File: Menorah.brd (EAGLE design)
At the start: 100 x 80 mm, 0 parts

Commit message: design finished
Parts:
- added C1: 100uF, rcl:C1808
- added G1: CR2032V, battery:CR2032V
- added IC1: (no value), linear:SO08
- added LED1, LED2, LED3, LED4, LED5, LED6, LED7, LED8, LED9: (no value), led:P-LCC-4
- added R1, R2, R3, R4, R5, R6, R7, R8, R9: (no value), rcl:R0805
- added R10: 10M, rcl:R0805
- added R11: 50k, rcl:R0805
- added R12: 100k, rcl:R0805
- added S1, S2, S3, S4, S5, S6, S7, S8, S9: 2P2T, switch:2P2T
- added S10: RDT1034, switch:RDT1034
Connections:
- new net N$1: LED1.A, R1.2
- new net N$10: R1.1, S1.3.2
- new net N$11: R2.1, S2.3.2
- new net N$12: R3.1, S3.3.2
- new net N$13: R4.1, S4.3.2
- new net N$14: R5.1, S5.3.2
- new net N$15: R6.1, S6.3.2
- new net N$16: R7.1, S7.3.2
- new net N$17: R8.1, S8.3.2
- new net N$18: R9.1, S9.3.2
- new net N$19: IC1.2, R11.1, R12.2
- new net N$2: LED2.A, R2.2
- new net N$20: C1.1, IC1.3, R10.2, S10.B
- new net N$21: IC1.6, S1.2.1
- new net N$23: S1.2.2, S2.2.1
- new net N$24: S2.2.2, S3.2.1
- new net N$25: S3.2.2, S4.2.1
- new net N$26: S4.2.2, S5.2.1
- new net N$27: S5.2.2, S6.2.1
- new net N$28: S6.2.2, S7.2.1
- new net N$29: S7.2.2, S8.2.1
- new net N$3: LED3.A, R3.2
- new net N$30: S8.2.2, S9.2.1
- new net N$4: LED4.A, R4.2
- new net N$5: LED5.A, R5.2
- new net N$6: LED6.A, R6.2
- new net N$7: LED7.A, R7.2
- new net N$8: LED8.A, R8.2
- new net N$9: LED9.A, R9.2
- new net PE: C1.2, G1.-, IC1.4, LED1.C@4, LED2.C@4, LED3.C@4, LED4.C@4, LED5.C@4, LED6.C@4, LED7.C@4, LED8.C@4, LED9.C@4, R10.1, R11.2
- new net VCC: G1.+, IC1.7, R12.1, S10.A, S10.A1

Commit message: digikey part numbers added
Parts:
- C1: device rcl:C1808 -> rcl:C1206
- LED1, LED2, LED3, LED4, LED5, LED6, LED7, LED8: value (none) -> YELLOW; device led:P-LCC-4 -> led:CHIPLED_0805
- LED9: value (none) -> RED; device led:P-LCC-4 -> led:CHIPLED_0805
- R1, R2, R3, R4, R5, R6, R7, R8: value (none) -> 56
- R11: value 50k -> 51k
- R9: value (none) -> 68
- moved S3 275.9 mm to (-152.4, -255.3)
- moved S4 275.9 mm to (-152.4, -268.0)
- moved S5 275.9 mm to (-152.4, -280.7)
- moved S6 275.9 mm to (-152.4, -293.4)
- moved S9 275.9 mm to (-152.4, -331.5)
- moved S2 275.9 mm to (-152.4, -242.6)
- moved S7 275.9 mm to (-152.4, -306.1)
- moved S8 275.9 mm to (-152.4, -318.8)
- moved R8 179.5 mm to (-157.5, -233.7)
- moved R7 178.9 mm to (-157.5, -227.3)
- moved R6 178.3 mm to (-157.5, -221.0)
- moved R5 177.8 mm to (-157.5, -214.6)
- moved R4 177.2 mm to (-157.5, -208.3)
- moved R3 176.7 mm to (-157.5, -201.9)
- moved R2 176.2 mm to (-157.5, -195.6)
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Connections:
- net PE: now also LED1.C, LED2.C, LED3.C, LED4.C, LED5.C, LED6.C, LED7.C, LED8.C, LED9.C; no longer LED1.C@4, LED2.C@4, LED3.C@4, LED4.C@4, LED5.C@4, LED6.C@4, LED7.C@4, LED8.C@4, LED9.C@4

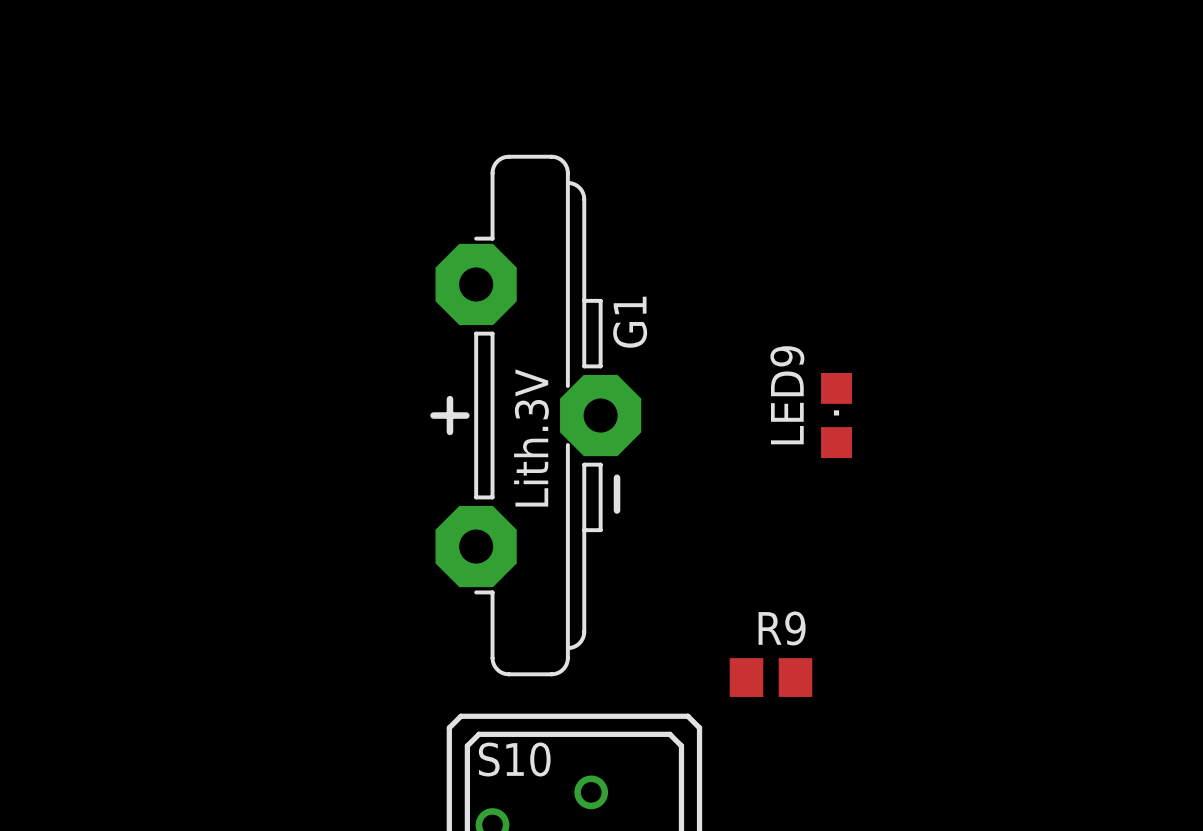
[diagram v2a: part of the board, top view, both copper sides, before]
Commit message: replaced cr2032
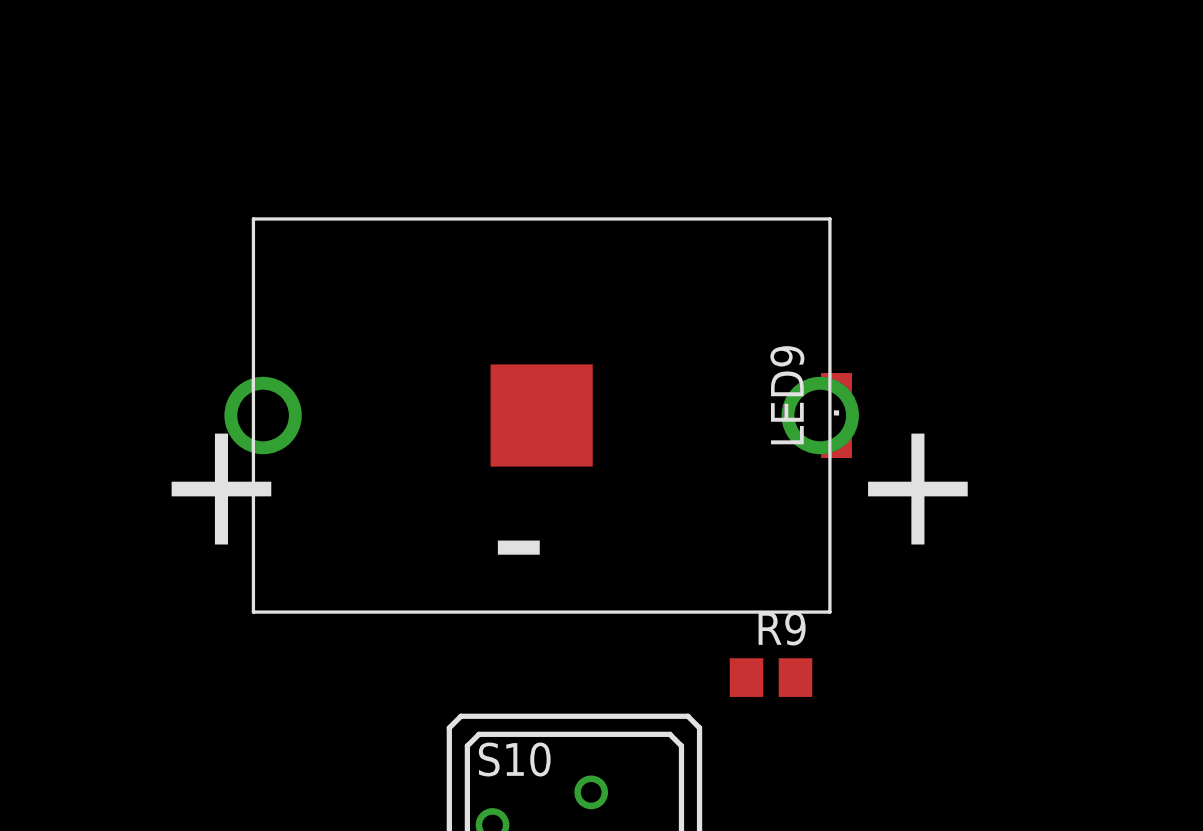
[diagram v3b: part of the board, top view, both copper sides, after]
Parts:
- G1: value CR2032V -> CR2032; device battery:CR2032V -> Menorah:BK-913
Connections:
- new net +: G1.+@1
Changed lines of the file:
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@@
 <attribute name="DIGIKEY" value="1276-5504-1-ND" x="-100.33" y="-157.48" size="1.778" layer="27" display="off"/>
 </element>
-<element name="G1" library="battery" package="CR2032V" value="CR2032V" x="-109.22" y="-147.32">
+<element name="G1" library="Menorah" package="BK-913" value="CR2032" x="-109.22" y="-147.32">
 <attribute name="DIGIKEY" value="BK-913-ND" x="-109.22" y="-147.32" size="1.778" layer="27" display="off"/>
+<attribute name="LAYOUT-VERIFIED" value="No" x="-109.22" y="-147.32" size="1.778" layer="27" display="off"/>
 </element>
 <element name="S10" library="switch" package="RDT1034" value="RDT1034" x="-107.95" y="-163.83">
 <attribute name="DIGIKEY" value="EG4791-ND" x="-107.95" y="-163.83" size="1.778" layer="27" display="off"/>
+<attribute name="LAYOUT-VERIFIED" value="No" x="-107.95" y="-163.83" size="1.778" layer="27" display="off"/>
 </element>
 <element name="C1" library="rcl" package="C1206" value="100uF" x="-110.49" y="-172.72">
@@
 <contactref element="LED7" pad="C"/>
 <contactref element="LED8" pad="C"/>
-<wire x1="-106.934" y1="-147.32" x2="-97.79" y2="-146.27" width="0" layer="19" extent="1-1"/>
-<wire x1="-109.09" y1="-172.72" x2="-106.934" y2="-147.32" width="0" layer="19" extent="1-1"/>
+<wire x1="-109.22" y1="-147.32" x2="-97.79" y2="-146.27" width="0" layer="19" extent="1-1"/>
+<wire x1="-109.09" y1="-172.72" x2="-109.22" y2="-147.32" width="0" layer="19" extent="1-1"/>
 <wire x1="-111.44" y1="-179.07" x2="-109.09" y2="-172.72" width="0" layer="19" extent="1-1"/>
 <wire x1="-109.54" y1="-184.15" x2="-111.44" y2="-179.07" width="0" layer="19" extent="1-1"/>
@@
 <wire x1="-111.125" y1="-163.195" x2="-118.745" y2="-177.74" width="0" layer="19" extent="1-1"/>
 <wire x1="-104.775" y1="-164.465" x2="-111.125" y2="-163.195" width="0" layer="19" extent="1-1"/>
-<wire x1="-111.76" y1="-152.4" x2="-111.125" y2="-163.195" width="0" layer="19" extent="1-1"/>
+<wire x1="-120.02" y1="-147.32" x2="-111.125" y2="-163.195" width="0" layer="19" extent="1-1"/>
 </signal>
 <signal name="N$19">
@@
 <wire x1="-152.4" y1="-321.42" x2="-152.4" y2="-328.82" width="0" layer="19" extent="1-1"/>
 </signal>
+<signal name="+">
+<contactref element="G1" pad="+@1"/>
+</signal>
 </signals>

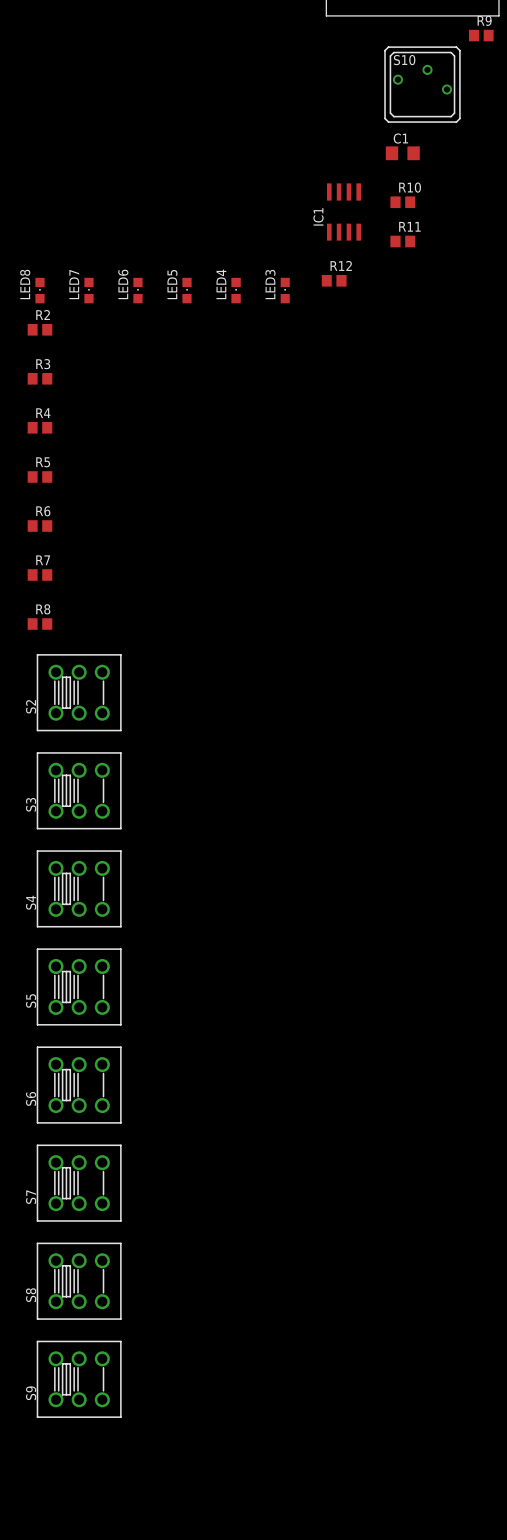
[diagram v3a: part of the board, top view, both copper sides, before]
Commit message: replaced spst switch
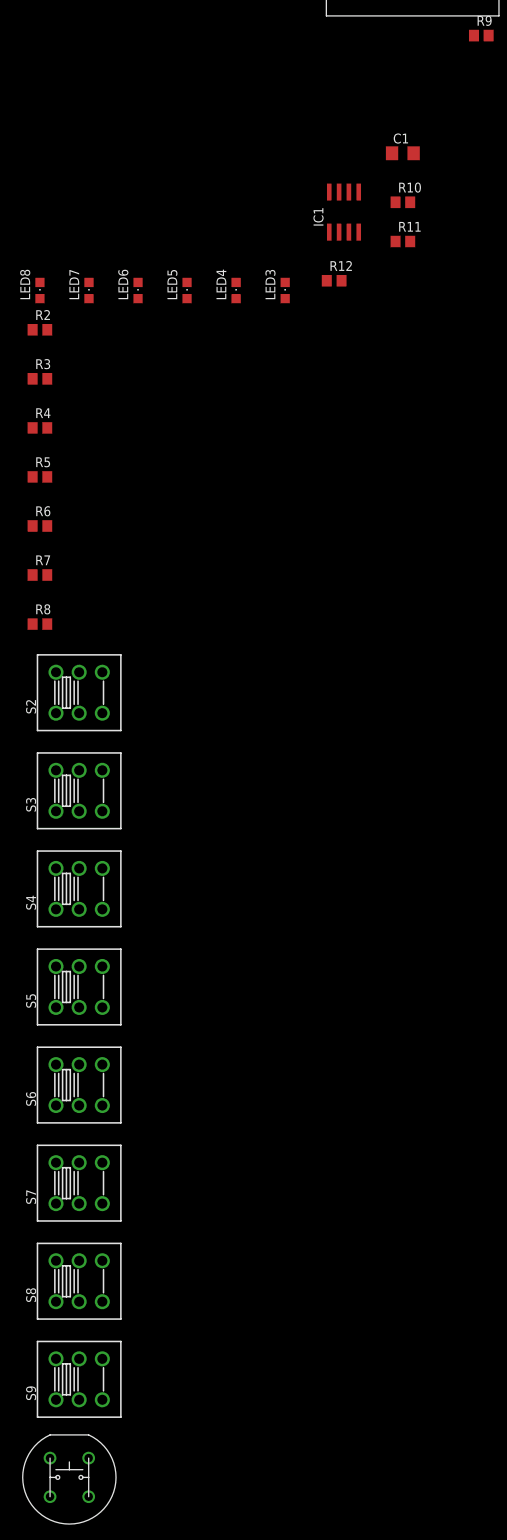
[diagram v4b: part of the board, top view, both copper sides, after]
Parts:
- S10: value RDT1034 -> SWITCH-SPST; device switch:RDT1034 -> Menorah:KS-01Q-01
- moved S10 186.0 mm to (-153.7, -344.2)
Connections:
- removed net N$20: C1.1, IC1.3, R10.2, S10.B
- new net N$22: C1.1, IC1.3, R10.2, S10.3, S10.4
- net VCC: now also S10.1, S10.2; no longer S10.A, S10.A1
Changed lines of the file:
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@@
 <element name="G1" library="Menorah" package="BK-913" value="CR2032" x="-109.22" y="-147.32">
 <attribute name="DIGIKEY" value="BK-913-ND" x="-109.22" y="-147.32" size="1.778" layer="27" display="off"/>
-<attribute name="LAYOUT-VERIFIED" value="No" x="-109.22" y="-147.32" size="1.778" layer="27" display="off"/>
-</element>
-<element name="S10" library="switch" package="RDT1034" value="RDT1034" x="-107.95" y="-163.83">
-<attribute name="DIGIKEY" value="EG4791-ND" x="-107.95" y="-163.83" size="1.778" layer="27" display="off"/>
-<attribute name="LAYOUT-VERIFIED" value="No" x="-107.95" y="-163.83" size="1.778" layer="27" display="off"/>
 </element>
 <element name="C1" library="rcl" package="C1206" value="100uF" x="-110.49" y="-172.72">
@@
 <attribute name="DIGIKEY" value="401-2002-1-ND" x="-152.4" y="-331.47" size="1.778" layer="27" display="off"/>
 </element>
+<element name="S10" library="Menorah" package="KS-01Q-01" value="SWITCH-SPST" x="-153.67" y="-344.17"/>
 </elements>
 <signals>
@@
 <wire x1="-6.35" y1="-146.27" x2="-17.78" y2="-146.27" width="0" layer="19" extent="1-1"/>
 </signal>
-<signal name="N$20">
-<contactref element="S10" pad="B"/>
-<contactref element="C1" pad="1"/>
-<contactref element="IC1" pad="3"/>
-<contactref element="R10" pad="2"/>
-<wire x1="-109.54" y1="-179.07" x2="-117.475" y2="-182.94" width="0" layer="19" extent="1-1"/>
-<wire x1="-111.89" y1="-172.72" x2="-109.54" y2="-179.07" width="0" layer="19" extent="1-1"/>
-<wire x1="-107.3" y1="-161.93" x2="-111.89" y2="-172.72" width="0" layer="19" extent="1-1"/>
-</signal>
 <signal name="VCC">
 <contactref element="G1" pad="+"/>
 <contactref element="IC1" pad="7"/>
 <contactref element="R12" pad="1"/>
-<contactref element="S10" pad="A1"/>
-<contactref element="S10" pad="A"/>
+<contactref element="S10" pad="1"/>
+<contactref element="S10" pad="2"/>
+<wire x1="-151.17" y1="-341.67" x2="-156.17" y2="-341.67" width="0" layer="19" extent="1-1"/>
+<wire x1="-120.33" y1="-189.23" x2="-151.17" y2="-341.67" width="0" layer="19" extent="1-1"/>
 <wire x1="-118.745" y1="-177.74" x2="-120.33" y2="-189.23" width="0" layer="19" extent="1-1"/>
-<wire x1="-111.125" y1="-163.195" x2="-118.745" y2="-177.74" width="0" layer="19" extent="1-1"/>
-<wire x1="-104.775" y1="-164.465" x2="-111.125" y2="-163.195" width="0" layer="19" extent="1-1"/>
-<wire x1="-120.02" y1="-147.32" x2="-111.125" y2="-163.195" width="0" layer="19" extent="1-1"/>
+<wire x1="-120.02" y1="-147.32" x2="-118.745" y2="-177.74" width="0" layer="19" extent="1-1"/>
 </signal>
 <signal name="N$19">
@@
 <contactref element="G1" pad="+@1"/>
 </signal>
+<signal name="N$22">
+<contactref element="S10" pad="4"/>
+<contactref element="S10" pad="3"/>
+<contactref element="C1" pad="1"/>
+<contactref element="IC1" pad="3"/>
+<contactref element="R10" pad="2"/>
+<wire x1="-151.17" y1="-346.67" x2="-156.17" y2="-346.67" width="0" layer="19" extent="1-1"/>
+<wire x1="-117.475" y1="-182.94" x2="-151.17" y2="-346.67" width="0" layer="19" extent="1-1"/>
+<wire x1="-109.54" y1="-179.07" x2="-117.475" y2="-182.94" width="0" layer="19" extent="1-1"/>
+<wire x1="-111.89" y1="-172.72" x2="-109.54" y2="-179.07" width="0" layer="19" extent="1-1"/>
+</signal>
 </signals>
